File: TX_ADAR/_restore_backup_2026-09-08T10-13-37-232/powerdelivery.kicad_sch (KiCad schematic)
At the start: 16 parts, among them IC1 REG1117A-1.8, IC2 REG1117A-2.5, SW10 SW_SPDT, SW11 SW_SPDT, SW2 SW_SPDT, SW9 SW_SPDT

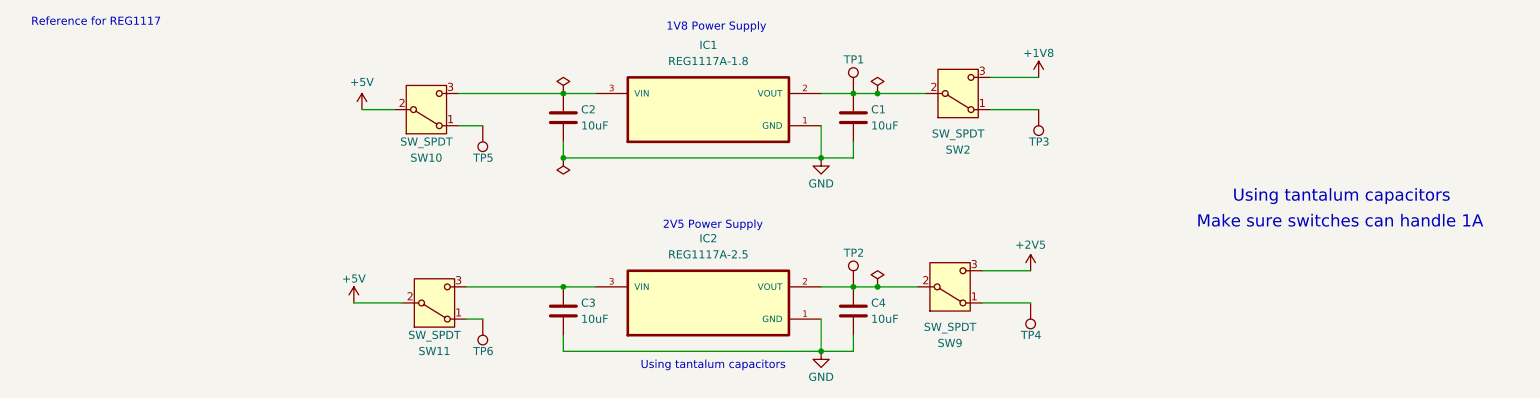
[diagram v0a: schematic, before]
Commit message: Some footprints updated and power buffers added
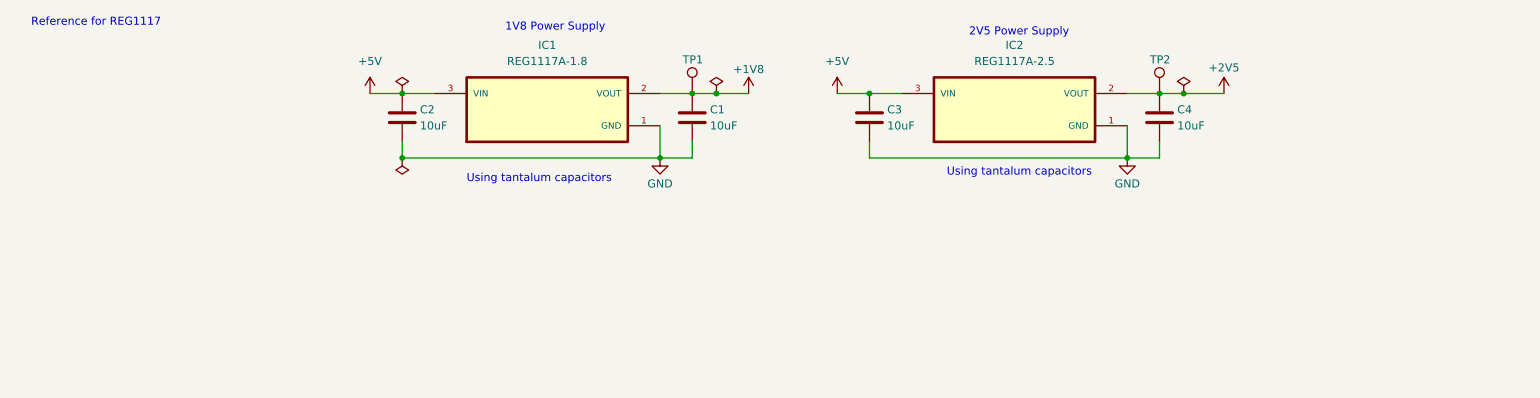
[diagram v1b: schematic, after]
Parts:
- removed SW10, SW11, SW2, SW9: SW_SPDT, symbol Switch:SW_SPDT
- removed TP3, TP4, TP5, TP6: TestPoint, symbol Connector:TestPoint
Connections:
- net +1V8: now also C1.1, IC1.2 (VOUT), TP1.1
- net +2V5: now also C4.1, IC2.2 (VOUT), TP2.1
- net +5V: now also C2.1, C3.1, IC1.3 (VIN), IC2.3 (VIN)
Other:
- note removed: "Make sure switches can handle 1A"
- moved on the sheet: C1, C2, C3, C4, IC1, IC2, TP1, TP2
